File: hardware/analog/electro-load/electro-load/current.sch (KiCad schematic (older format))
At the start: 21 parts, among them J3 Barrel_Jack, K1 SANYOU_SRD_Form_C, Q3 Q_NJFET_GDS, Q4 2N2222, U6 LM358DR

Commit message: HW rev 1 of electronic load PCB.
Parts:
- removed C16: 100n 25V, Capacitor_SMD:C_0603_1608Metric, symbol Device:C_Small
- removed D4: D_Schottky, athir:SOD80C(Reflow), symbol Device:D_Schottky
- removed D?: 5+V protection, symbol Device:D_Zener
- removed Q4: 2N2222, Package_TO_SOT_THT:TO-92_Inline, symbol dk_Transistors-Bipolar-BJT-Single:2N2222
- removed U6: LM358DR, digikey-footprints:SOIC-8_W3.9mm, symbol dk_Linear-Amplifiers-Instrumentation-OP-Amps-Buffer-Amps:LM358DR
- added C14: 1n, Capacitor_SMD:C_0603_1608Metric, symbol Device:C_Small
- added D6: flyback, Diode_THT:D_DO-35_SOD27_P7.62mm_Horizontal, symbol Device:D_Zener_Small
- added D7: 5+V protection, Diode_THT:D_DO-35_SOD27_P7.62mm_Horizontal, symbol Device:D_Zener
- added HS1: RS_176-4176, athir:Heatsink_Fischer_SK104-STC-STIC_35x13mm_2xDrill2.5mm, symbol Mechanical:Heatsink
- added Q4: IPP055N03L G, Package_TO_SOT_THT:TO-220-3_Vertical, symbol Device:Q_NJFET_GDS
- added Q5: 2N2222, Package_TO_SOT_THT:TO-92_Inline, symbol dk_Transistors-Bipolar-BJT-Single:2N2222
- added R18, R20, R21, R23: 1R 100W, TestPoint:TestPoint_2Pads_Pitch5.08mm_Drill1.3mm, symbol Device:R_US
- added R19, R22, R32: 1k, Resistor_SMD:R_0603_1608Metric, symbol Device:R_Small
- added RV5, RV8: 6k8 POT, Potentiometer_THT:Potentiometer_Bourns_3296W_Vertical, symbol Device:R_POT
- added RV6: 2k POT, Potentiometer_THT:Potentiometer_Bourns_3296W_Vertical, symbol Device:R_POT
- added RV7: 10k POT, Potentiometer_THT:Potentiometer_Bourns_3296W_Vertical, symbol Device:R_POT
- added TP6, TP7, TP8, TP9: TestPoint, athir:testpoint_probe, symbol Connector:TestPoint
- added U6: LMV324, Package_SO:SOIC-14_3.9x8.7mm_P1.27mm, symbol Amplifier_Operational:LMV324
- C15: value 100n 25V -> 100n
- J3: value Barrel_Jack -> INPUT
- Q3: value Q_NJFET_GDS -> IPP055N03L G (NM); footprint Package_TO_SOT_SMD:TO-263-2 -> Package_TO_SOT_THT:TO-220-3_Vertical
- R24: value 1k -> 10k
- R25: value 10M 1% -> 825R
- R26: value 1M5 1% -> 100
- R27: value 2M -> 1k
- R28: value 825k -> 1k5
- R29: value 2R 128++W -> 1k; footprint TestPoint:TestPoint_2Pads_Pitch5.08mm_Drill1.3mm -> Resistor_SMD:R_0603_1608Metric
- R30: value 2ohm 128++W -> 1k; footprint TestPoint:TestPoint_2Pads_Pitch5.08mm_Drill1.3mm -> Resistor_SMD:R_0603_1608Metric
- R31: value 4k7 -> 1k
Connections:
- net labels added: V_MEAS
- net labels removed: VCC, V_IN
- wire segments 89 -> 144
- no-connect marks 1 -> 5
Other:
- note removed: "OBS: 2N2222A vs -A har forskelligt PINOUT!!"

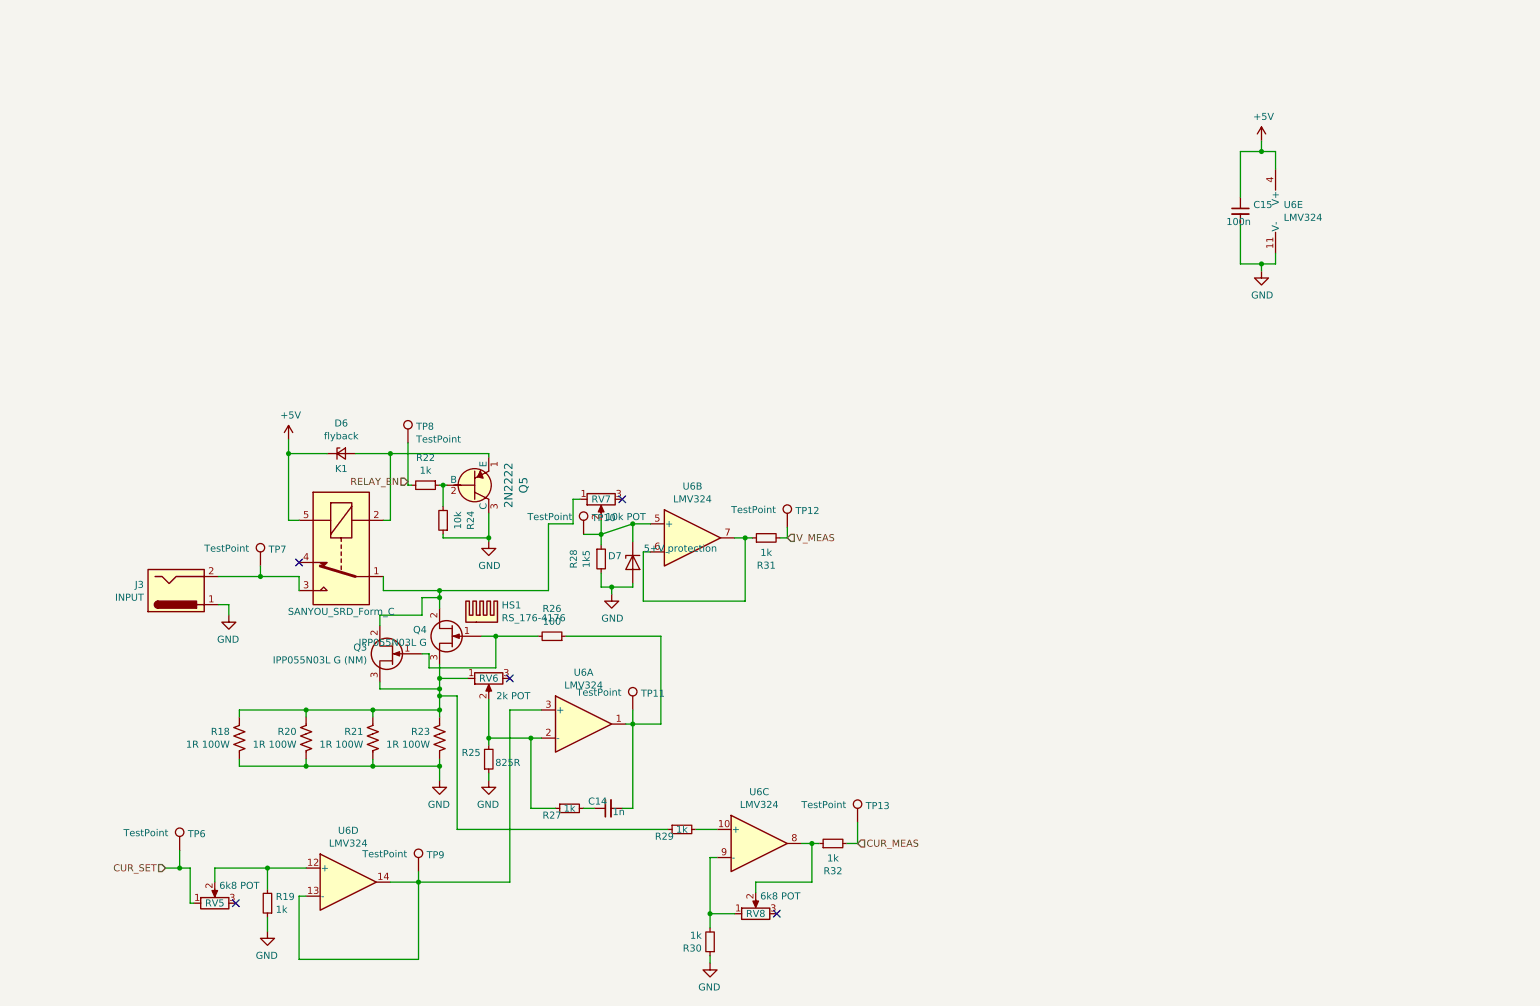
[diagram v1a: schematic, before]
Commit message: Added voltage reference REF5020 datasheet
Started work on HW rev 2 of electro load and 5v-from-mains - rev 1 contained misaligned footprints.
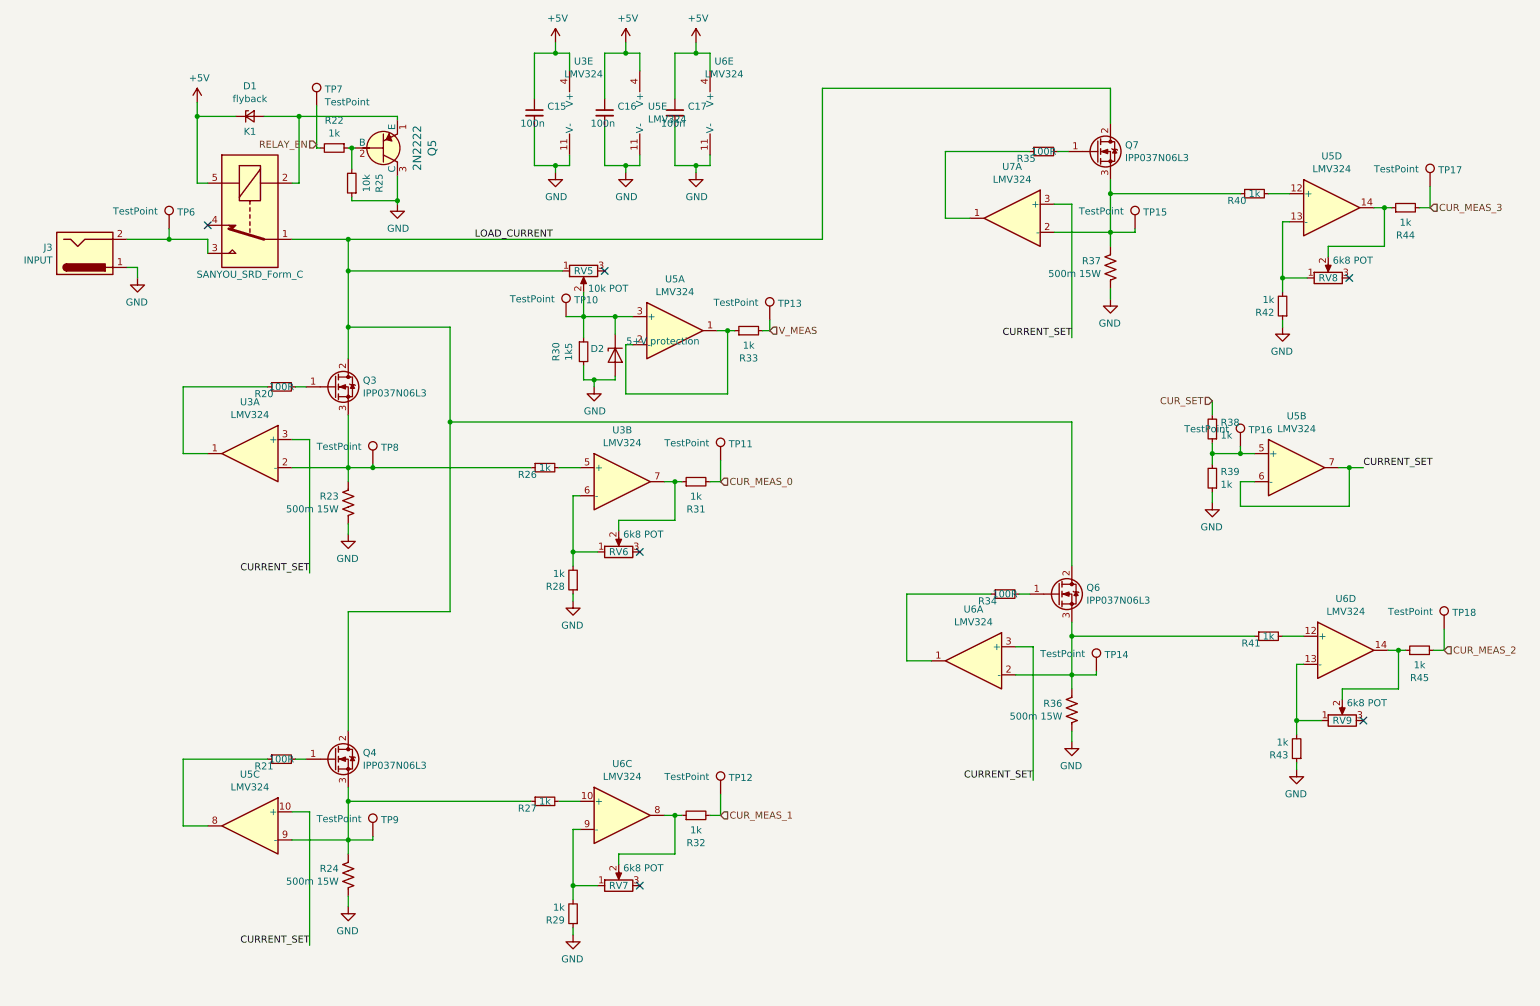
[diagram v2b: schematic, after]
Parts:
- removed C14: 1n, Capacitor_SMD:C_0603_1608Metric, symbol Device:C_Small
- removed HS1: RS_176-4176, athir:Heatsink_Fischer_SK104-STC-STIC_35x13mm_2xDrill2.5mm, symbol Mechanical:Heatsink
- removed Q3: IPP055N03L G (NM), Package_TO_SOT_THT:TO-220-3_Vertical, symbol Device:Q_NJFET_GDS
- removed Q4: IPP055N03L G, Package_TO_SOT_THT:TO-220-3_Vertical, symbol Device:Q_NJFET_GDS
- removed R19, R27: 1k, Resistor_SMD:R_0603_1608Metric, symbol Device:R_Small
- removed R20, R21, R23: 1R 100W, TestPoint:TestPoint_2Pads_Pitch5.08mm_Drill1.3mm, symbol Device:R_US
- removed R25: 825R, Resistor_SMD:R_0603_1608Metric, symbol Device:R_Small
- removed RV5: 6k8 POT, Potentiometer_THT:Potentiometer_Bourns_3296W_Vertical, symbol Device:R_POT
- removed TP6: TestPoint, athir:testpoint_probe, symbol Connector:TestPoint
- added C15, C17: 100n, Capacitor_SMD:C_0603_1608Metric, symbol Device:C_Small
- added Q3, Q4, Q6, Q7: IPP037N06L3, Package_TO_SOT_THT:TO-220-3_Vertical, symbol Device:Q_NMOS_GDS
- added R20, R21, R34, R35: 100R, Resistor_SMD:R_0603_1608Metric, symbol Device:R_Small
- added R24, R36, R37: 500m 15W, TestPoint:TestPoint_2Pads_Pitch5.08mm_Drill1.3mm, symbol Device:R_US
- added R28, R31, R38, R39, R40, R41, R42, R43, R44, R45: 1k, Resistor_SMD:R_0603_1608Metric, symbol Device:R_Small
- added RV8, RV9: 6k8 POT, Potentiometer_THT:Potentiometer_Bourns_3296W_Vertical, symbol Device:R_POT
- added TP14, TP15, TP16, TP17, TP18, TP9: TestPoint, athir:testpoint_probe, symbol Connector:TestPoint
- added U3, U7: LMV324, Package_SO:SOIC-14_3.9x8.7mm_P1.27mm, symbol Amplifier_Operational:LMV324
- added unit 2 of U5
- added unit 4 of U5
- added unit 3 of U5
- added unit 5 of U6
- R23: renamed from R18; value 1R 100W -> 500m 15W
- R26: value 100 -> 1k
- RV6: value 2k POT -> 6k8 POT
- renumbered C15 to C16, D6 to D1, D7 to D2, R24 to R25, R29 to R27, R30 to R29, R28 to R30, R31 to R33, RV7 to RV5, RV8 to RV7, TP13 to TP12, TP12 to TP13, TP7 to TP6, TP8 to TP7, TP9 to TP8, U6 to U5
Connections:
- net +5V: now also C15.1, C17.1, U3.4 (V+), U6.4 (V+)
- net CUR_SET: now also R38.2
- net GND: now also C15.2, C17.2, R24.2, R28.1, R36.2, R37.2, R39.1, R42.1, R43.1, U3.11 (V-), U6.11 (V-)
- net at U6.12 (+): now also R41.2
- net LOAD_CURRENT: now reaches K1.1, RV5.1
- net LOAD_CURRENT: now also Q3.2 (D), Q4.2 (D), Q6.2 (D), Q7.2 (D)
- net at RV6.2: now also R31.1, U3.7; no longer U6.2 (-)
- net at R26.2: now also U3.5 (+)
- net at D2.1 (K), R30.1, RV5.2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: now also U5.3 (+); no longer U5.5 (+)
- net CUR_MEAS renamed CUR_MEAS_1
- new net: Q3.3 (S), R23.1, R26.1, TP8.1, U3.2 (-)
- new net: R33.1, U5.1, U5.2 (-)
- new net: Q3.1 (G), R20.2
- new net: R20.1, U3.1
- new net: Q7.3 (S), R37.1, R40.1, TP15.1, U7.2 (-)
- new net: Q7.1 (G), R35.2
- new net: R35.1, U7.1
- new net: R38.1, R39.2, TP16.1, U5.5 (+)
- new net: R42.2, RV8.1, U5.13 (-)
- new net: R40.2, U5.12 (+)
- new net: R44.1, RV8.2, U5.14
- new net: Q4.3 (S), R24.1, R27.1, TP9.1, U5.9 (-)
- new net: Q4.1 (G), R21.2
- new net: R21.1, U5.8
- new net: R28.2, RV6.1, U3.6 (-)
- new net: Q6.3 (S), R36.1, R41.1, TP14.1, U6.2 (-)
- new net: Q6.1 (G), R34.2
- new net: R34.1, U6.1
- new net: R43.2, RV9.1, U6.13 (-)
- new net: R45.1, RV9.2, U6.14
- new net CURRENT_SET: U3.3 (+), U5.10 (+), U5.6 (-), U5.7, U6.3 (+), U7.3 (+)
- new net CUR_MEAS_0: R31.2, TP11.1
- new net CUR_MEAS_2: R45.2, TP18.1
- new net CUR_MEAS_3: R44.2, TP17.1
- no-connect marks 5 -> 6
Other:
- moved on the sheet: C16, D1, D2, J3, K1, Q5, R22, R23, R25, R27, R29, R30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

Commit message: Changed pin connections to/from lmv324 in order to avoid bird nesting. Widened traces for 5V and LOAD_CURRENT. Added four power resistors to the fab layer. Arranged left side analogs
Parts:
- removed TP14, TP15, TP8, TP9: TestPoint, athir:testpoint_probe, symbol Connector:TestPoint
- added J4: INPUT, TestPoint:TestPoint_2Pads_Pitch5.08mm_Drill1.3mm, symbol Connector:Barrel_Jack
- renumbered U5 to U3, U6 to U3, U7 to U6, U5 to U6
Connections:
- net CURRENT_SET: now also U6.5 (+); no longer U6.3 (+)
- net GND: now also J4.1
- net at J3.2, K1.3, TP6.1: now also J4.2
- net at R29.2, RV7.1: now also U3.13 (-); no longer U3.9 (-)
- net at Q7.3 (S), R37.1, R40.1: now also U6.6 (-); no longer U6.2 (-)
- net at R35.1: now also U6.7; no longer U6.1
- net at R42.2, RV8.1: now also U6.9 (-); no longer U6.13 (-)
- net at R40.2: now also U6.10 (+); no longer U6.12 (+)
- net at R44.1, RV8.2: now also U6.8; no longer U6.14
- net at R27.2: now also U3.12 (+); no longer U3.10 (+)
- net at R32.1, RV7.2: now also U3.14; no longer U3.8
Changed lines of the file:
@@
 $Descr A4 11693 8268
 encoding utf-8
-Sheet 5 5
+Sheet 4 5
 Title ""
 Date ""
@@
 $EndComp
 Wire Wire Line
-	1375 2150 1675 2150
+	1375 2150 1550 2150
 NoConn ~ 1950 2050
 $Comp
@@
 $EndComp
 $Comp
-L Amplifier_Operational:LMV324 U6
-U 3 1 5ED474FC
+L Amplifier_Operational:LMV324 U3
+U 4 1 5ED474FC
 P 4900 6250
-F 0 "U6" H 4900 6617 50  0000 C CNN
+F 0 "U3" H 4900 6617 50  0000 C CNN
 F 1 "LMV324" H 4900 6526 50  0000 C CNN
 F 2 "Package_SO:SOIC-14_3.9x8.7mm_P1.27mm" H 4850 6350 50  0001 C CNN
 F 3 "http://www.ti.com/lit/ds/symlink/lmv324.pdf" H 4950 6450 50  0001 C CNN
-	3    4900 6250
+	4    4900 6250
 	1    0    0    -1
 $EndComp
@@
 Wire Wire Line
 	4500 2700 4625 2700
-$Comp
-L Connector:TestPoint TP?
-U 1 1 5ED9DFFE
-P 3125 3750
-AR Path="/5ED9DFFE" Ref="TP?"  Part="1"
-AR Path="/5E82E2D2/5ED9DFFE" Ref="TP8"  Part="1"
-F 0 "TP8" H 3183 3868 50  0000 L CNN
-F 1 "TestPoint" H 2725 3875 50  0000 L CNN
-F 2 "athir:testpoint_probe" H 3325 3750 50  0001 C CNN
-F 3 "~" H 3325 3750 50  0001 C CNN
-	1    3125 3750
-	1    0    0    -1
-$EndComp
 $Comp
 L Connector:TestPoint TP?
@@
 	2675 6225 2550 6225
 Wire Wire Line
-	3125 3750 3125 3775
-Wire Wire Line
-	3125 3775 2950 3775
-Wire Wire Line
 	2950 4800 3675 4800
 Wire Wire Line
@@
 Wire Wire Line
 	2950 2775 2950 3000
-$Comp
-L Connector:TestPoint TP?
-U 1 1 5EB3C700
-P 3125 6400
-AR Path="/5EB3C700" Ref="TP?"  Part="1"
-AR Path="/5E82E2D2/5EB3C700" Ref="TP9"  Part="1"
-F 0 "TP9" H 3183 6518 50  0000 L CNN
-F 1 "TestPoint" H 2725 6525 50  0000 L CNN
-F 2 "athir:testpoint_probe" H 3325 6400 50  0001 C CNN
-F 3 "~" H 3325 6400 50  0001 C CNN
-	1    3125 6400
-	1    0    0    -1
-$EndComp
-Wire Wire Line
-	3125 6400 3125 6425
-Wire Wire Line
-	3125 6425 2950 6425
 Wire Wire Line
 	2950 2375 4475 2375
@@
 Text HLabel 5600 3875 2    50   Input ~ 0
 CUR_MEAS_0
-Connection ~ 3125 3775
-Wire Wire Line
-	3125 3775 4250 3775
 Wire Wire Line
 	2950 6150 4250 6150
@@
 Wire Wire Line
 	7825 5050 7700 5050
-$Comp
-L Connector:TestPoint TP?
-U 1 1 5EC32B23
-P 8275 5225
-AR Path="/5EC32B23" Ref="TP?"  Part="1"
-AR Path="/5E82E2D2/5EC32B23" Ref="TP14"  Part="1"
-F 0 "TP14" H 8333 5343 50  0000 L CNN
-F 1 "TestPoint" H 7875 5350 50  0000 L CNN
-F 2 "athir:testpoint_probe" H 8475 5225 50  0001 C CNN
-F 3 "~" H 8475 5225 50  0001 C CNN
-	1    8275 5225
-	1    0    0    -1
-$EndComp
-Wire Wire Line
-	8275 5225 8275 5250
-Wire Wire Line
-	8275 5250 8100 5250
 Wire Wire Line
 	8100 4975 9400 4975
@@
 Wire Wire Line
 	8375 2575 8375 2500
-$Comp
-L Amplifier_Operational:LMV324 U5
-U 2 1 5E9BC375
-P 9700 3775
-F 0 "U5" H 9700 4142 50  0000 C CNN
-F 1 "LMV324" H 9700 4051 50  0000 C CNN
-F 2 "Package_SO:SOIC-14_3.9x8.7mm_P1.27mm" H 9650 3875 50  0001 C CNN
-F 3 "http://www.ti.com/lit/ds/symlink/lmv324.pdf" H 9750 3975 50  0001 C CNN
-	2    9700 3775
-	1    0    0    -1
-$EndComp
 Wire Wire Line
 	10000 3775 10075 3775
@@
 Wire Wire Line
 	9300 3675 9400 3675
-$Comp
-L Connector:TestPoint TP?
-U 1 1 5E9BC3B9
-P 8550 2075
-AR Path="/5E9BC3B9" Ref="TP?"  Part="1"
-AR Path="/5E82E2D2/5E9BC3B9" Ref="TP15"  Part="1"
-F 0 "TP15" H 8608 2193 50  0000 L CNN
-F 1 "TestPoint" H 8150 2200 50  0000 L CNN
-F 2 "athir:testpoint_probe" H 8750 2075 50  0001 C CNN
-F 3 "~" H 8750 2075 50  0001 C CNN
-	1    8550 2075
-	1    0    0    -1
-$EndComp
-Wire Wire Line
-	8550 2075 8550 2100
-Wire Wire Line
-	8550 2100 8375 2100
 Connection ~ 8375 1825
 Wire Wire Line
@@
 	10575 1925 10650 1925
 $Comp
-L Amplifier_Operational:LMV324 U5
-U 4 1 5E9BC3FC
+L Amplifier_Operational:LMV324 U6
+U 3 1 5E9BC3FC
 P 9950 1925
-F 0 "U5" H 9950 2292 50  0000 C CNN
+F 0 "U6" H 9950 2292 50  0000 C CNN
 F 1 "LMV324" H 9950 2201 50  0000 C CNN
 F 2 "Package_SO:SOIC-14_3.9x8.7mm_P1.27mm" H 9900 2025 50  0001 C CNN
 F 3 "http://www.ti.com/lit/ds/symlink/lmv324.pdf" H 10000 2125 50  0001 C CNN
-	4    9950 1925
+	3    9950 1925
 	1    0    0    -1
 $EndComp
@@
 $EndComp
 $Comp
-L Amplifier_Operational:LMV324 U7
-U 1 1 5E9BC359
+L Amplifier_Operational:LMV324 U6
+U 2 1 5E9BC359
 P 7675 2000
-F 0 "U7" H 7675 2367 50  0000 C CNN
+F 0 "U6" H 7675 2367 50  0000 C CNN
 F 1 "LMV324" H 7675 2276 50  0000 C CNN
 F 2 "Package_SO:SOIC-14_3.9x8.7mm_P1.27mm" H 7625 2100 50  0001 C CNN
 F 3 "http://www.ti.com/lit/ds/symlink/lmv324.pdf" H 7725 2200 50  0001 C CNN
-	1    7675 2000
-	-1   0    0    -1
-$EndComp
-$Comp
-L Amplifier_Operational:LMV324 U5
+	2    7675 2000
+	-1   0    0    -1
+$EndComp
+$Comp
+L Amplifier_Operational:LMV324 U3
 U 3 1 5EA3DD42
 P 2250 6325
-F 0 "U5" H 2250 6692 50  0000 C CNN
+F 0 "U3" H 2250 6692 50  0000 C CNN
 F 1 "LMV324" H 2250 6601 50  0000 C CNN
 F 2 "Package_SO:SOIC-14_3.9x8.7mm_P1.27mm" H 2200 6425 50  0001 C CNN
@@
 Text Label 3850 2150 0    50   ~ 0
 LOAD_CURRENT
+$Comp
+L Amplifier_Operational:LMV324 U5
+U 2 1 5E9BC375
+P 9700 3775
+F 0 "U5" H 9700 4142 50  0000 C CNN
+F 1 "LMV324" H 9700 4051 50  0000 C CNN
+F 2 "Package_SO:SOIC-14_3.9x8.7mm_P1.27mm" H 9650 3875 50  0001 C CNN
+F 3 "http://www.ti.com/lit/ds/symlink/lmv324.pdf" H 9750 3975 50  0001 C CNN
+	2    9700 3775
+	1    0    0    -1
+$EndComp
+Wire Wire Line
+	2950 3775 4250 3775
+$Comp
+L Connector:Barrel_Jack J?
+U 1 1 5EBBF432
+P 1050 1825
+AR Path="/5EBBF432" Ref="J?"  Part="1"
+AR Path="/5E82E2D2/5EBBF432" Ref="J4"  Part="1"
+F 0 "J4" H 820 1783 50  0000 R CNN
+F 1 "INPUT" H 820 1874 50  0000 R CNN
+F 2 "TestPoint:TestPoint_2Pads_Pitch5.08mm_Drill1.3mm" H 1100 1785 50  0001 C CNN
+F 3 "~" H 1100 1785 50  0001 C CNN
+	1    1050 1825
+	1    0    0    1
+$EndComp
+Wire Wire Line
+	1350 1925 1450 1925
+Wire Wire Line
+	1450 1925 1450 2350
+Connection ~ 1450 2350
+Wire Wire Line
+	1350 1725 1550 1725
+Wire Wire Line
+	1550 1725 1550 2150
+Connection ~ 1550 2150
+Wire Wire Line
+	1550 2150 1675 2150
 $EndSCHEMATC

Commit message: Sorry future me
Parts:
- removed Q5: 2N2222, Package_TO_SOT_THT:TO-92_Inline, symbol dk_Transistors-Bipolar-BJT-Single:2N2222
- added Q?: 2N3904, digikey-footprints:TO-92-3, symbol dk_Transistors-Bipolar-BJT-Single:2N3904
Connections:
- net GND: now also Q?.1 (E)
- net at D1.2 (A), K1.2: now also Q?.2 (C)
- net at R22.1, R25.2: now also Q?.3 (B)
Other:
- note added: "Rettet fra Rev 2 - C og E var byttet\n"
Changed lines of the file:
@@
-	1    0    0    -1
-$EndComp
-$Comp
-L dk_Transistors-Bipolar-BJT-Single:2N2222 Q?
-U 1 1 5EAD9292
-P 3200 1500
-AR Path="/5EAD9292" Ref="Q?"  Part="1"
-AR Path="/5E82E2D2/5EAD9292" Ref="Q5"  Part="1"
-F 0 "Q5" V 3547 1500 60  0000 C CNN
-F 1 "2N2222" V 3441 1500 60  0000 C CNN
-F 2 "Package_TO_SOT_THT:TO-92_Inline" H 3400 1700 60  0001 L CNN
-F 3 "https://my.centralsemi.com/get_document.php?cmp=1&mergetype=pd&mergepath=pd&pdf_id=2N2221.PDF" H 3400 1800 60  0001 L CNN
-F 4 "2N2222CS-ND" H 3400 1900 60  0001 L CNN "Digi-Key_PN"
-F 5 "2N2222" H 3400 2000 60  0001 L CNN "MPN"
-F 6 "Discrete Semiconductor Products" H 3400 2100 60  0001 L CNN "Category"
-F 7 "Transistors - Bipolar (BJT) - Single" H 3400 2200 60  0001 L CNN "Family"
-F 8 "https://my.centralsemi.com/get_document.php?cmp=1&mergetype=pd&mergepath=pd&pdf_id=2N2221.PDF" H 3400 2300 60  0001 L CNN "DK_Datasheet_Link"
-F 9 "/product-detail/en/central-semiconductor-corp/2N2222/2N2222CS-ND/4806844" H 3400 2400 60  0001 L CNN "DK_Detail_Page"
-F 10 "TRANS NPN 30V 0.8A TO-18" H 3400 2500 60  0001 L CNN "Description"
-F 11 "Central Semiconductor Corp" H 3400 2600 60  0001 L CNN "Manufacturer"
-F 12 "Active" H 3400 2700 60  0001 L CNN "Status"
-	1    3200 1500
 	1    0    0    -1
 $EndComp
@@
 Wire Wire Line
 	1550 2150 1675 2150
+$Comp
+L dk_Transistors-Bipolar-BJT-Single:2N3904 Q?
+U 1 1 5EC1DD71
+P 3200 1500
+F 0 "Q?" H 3388 1553 60  0000 L CNN
+F 1 "2N3904" H 3388 1447 60  0000 L CNN
+F 2 "digikey-footprints:TO-92-3" H 3400 1700 60  0001 L CNN
+F 3 "https://my.centralsemi.com/get_document.php?cmp=1&mergetype=pd&mergepath=pd&pdf_id=LSSGP072.PDF" H 3400 1800 60  0001 L CNN
+F 4 "2N3904CS-ND" H 3400 1900 60  0001 L CNN "Digi-Key_PN"
+F 5 "2N3904" H 3400 2000 60  0001 L CNN "MPN"
+F 6 "Discrete Semiconductor Products" H 3400 2100 60  0001 L CNN "Category"
+F 7 "Transistors - Bipolar (BJT) - Single" H 3400 2200 60  0001 L CNN "Family"
+F 8 "https://my.centralsemi.com/get_document.php?cmp=1&mergetype=pd&mergepath=pd&pdf_id=LSSGP072.PDF" H 3400 2300 60  0001 L CNN "DK_Datasheet_Link"
+F 9 "/product-detail/en/central-semiconductor-corp/2N3904/2N3904CS-ND/4806876" H 3400 2400 60  0001 L CNN "DK_Detail_Page"
+F 10 "TRANS NPN 40V TO-92" H 3400 2500 60  0001 L CNN "Description"
+F 11 "Central Semiconductor Corp" H 3400 2600 60  0001 L CNN "Manufacturer"
+F 12 "Active" H 3400 2700 60  0001 L CNN "Status"
+	1    3200 1500
+	1    0    0    -1
+$EndComp
+Text Notes 2500 1575 0    50   ~ 0
+Rettet fra Rev 2 - C og E var byttet\n
 $EndSCHEMATC
